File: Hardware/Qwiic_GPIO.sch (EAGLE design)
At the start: 31 parts, among them J2 SMD, J3 PTH, J4 SMD, U3 TCA9534U

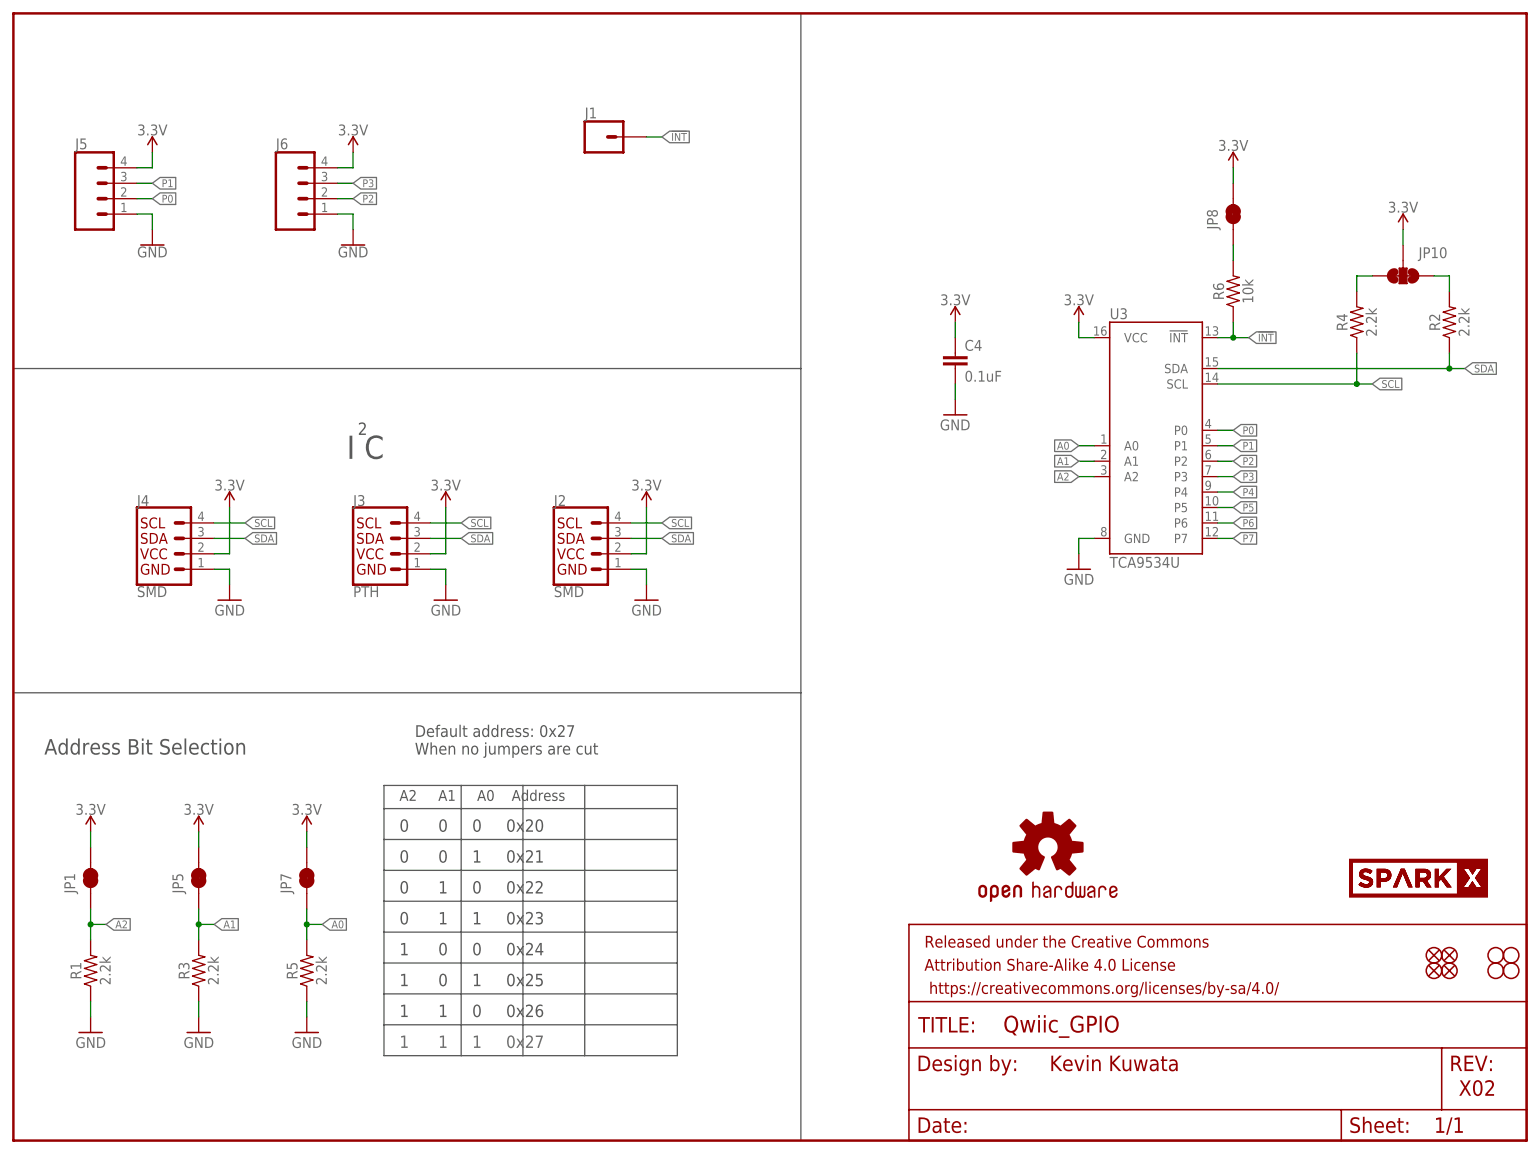
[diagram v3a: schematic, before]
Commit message: Change silk to table
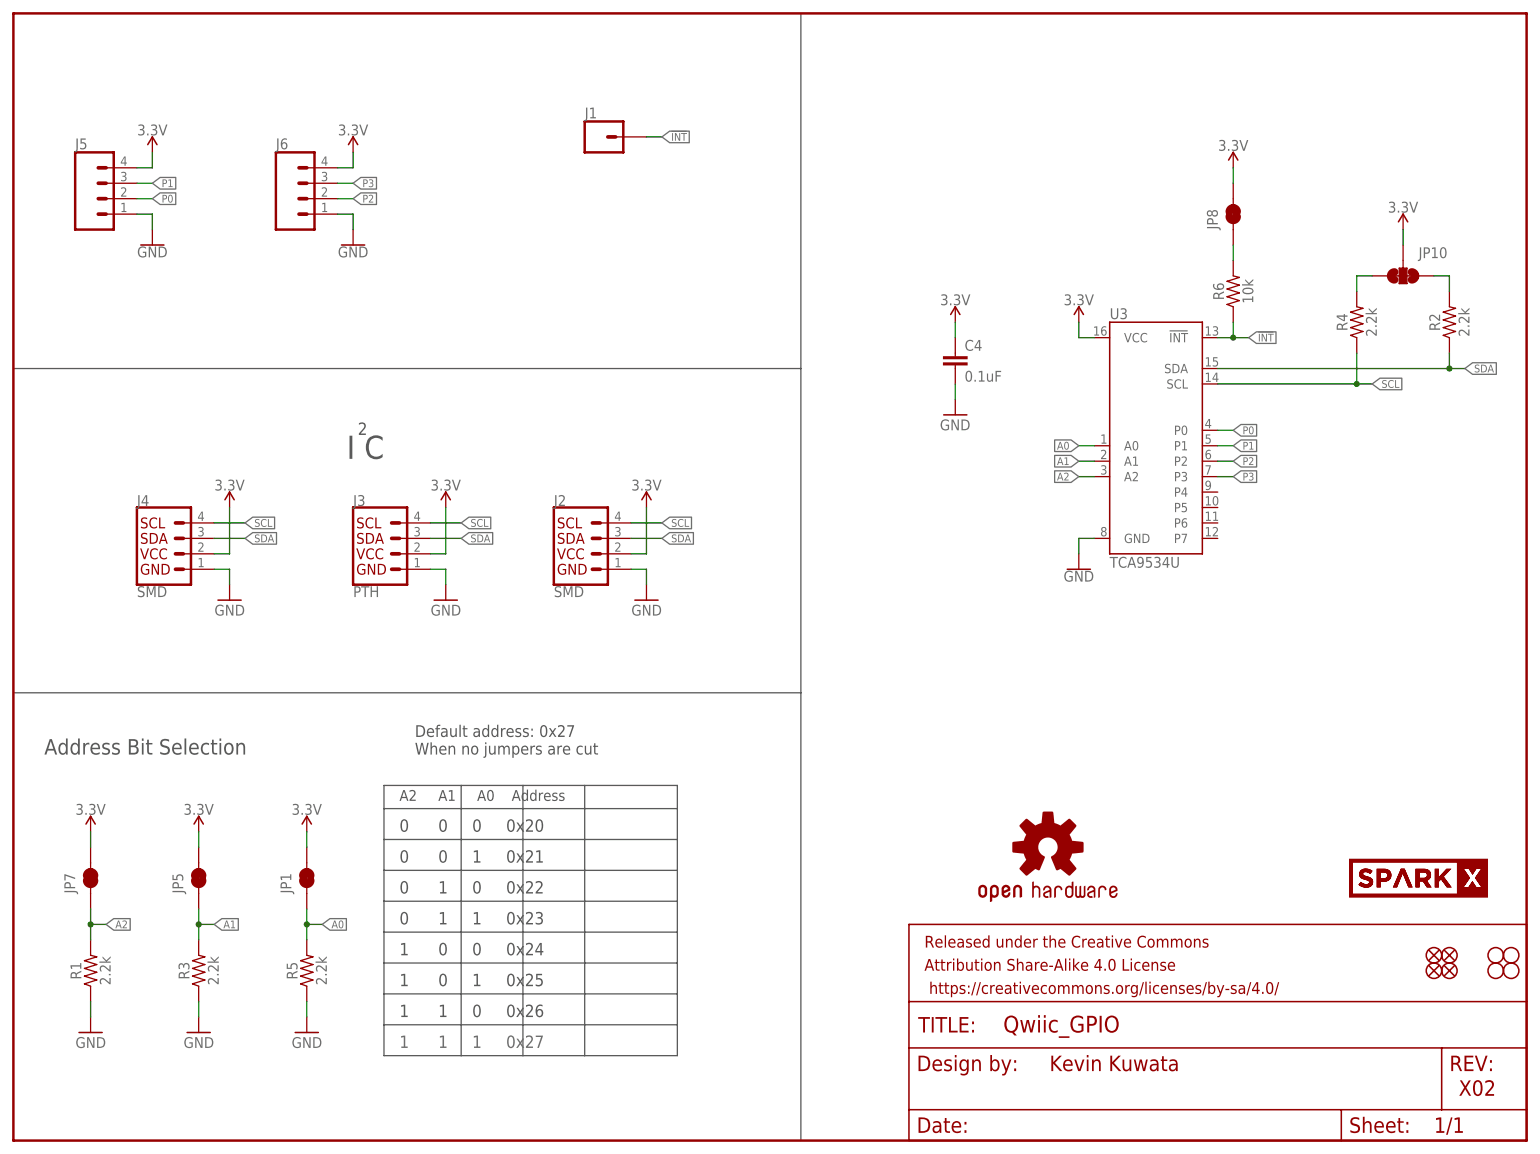
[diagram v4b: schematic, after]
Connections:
- removed net P4: U3.P4
- removed net P5: U3.P5
- removed net P6: U3.P6
- removed net P7: U3.P7
- net A0: now also JP1.1; no longer JP7.1
- net A2: now also JP7.1; no longer JP1.1
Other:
- moved on the sheet: JP1, JP7
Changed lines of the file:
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@@
 <?xml version="1.0" encoding="utf-8"?>
 <!DOCTYPE eagle SYSTEM "eagle.dtd">
-<eagle version="9.4.2">
+<eagle version="9.5.2">
 <drawing>
 <settings>
@@
 <part name="U3" library="KevinKuwata_eagle" deviceset="TCA9534" device="U"/>
 <part name="J1" library="SparkFun-Connectors" deviceset="CONN_01" device="PTH_NO_SILK_YES_STOP"/>
-<part name="JP1" library="SparkFun-Jumpers" deviceset="JUMPER-SMT_2_NC_TRACE" device="_SILK" package3d_urn="urn:adsk.eagle:package:39281/1" value="JUMPER-SMT_2_NC_TRACE_SILK"/>
 <part name="R1" library="SparkFun-Resistors" deviceset="2.2KOHM" device="-0603-1/10W-1%" value="2.2k"/>
 <part name="R3" library="SparkFun-Resistors" deviceset="2.2KOHM" device="-0603-1/10W-1%" value="2.2k"/>
@@
 <part name="GND2" library="SparkFun" deviceset="GND" device=""/>
 <part name="GND3" library="SparkFun" deviceset="GND" device=""/>
-<part name="JP5" library="SparkFun-Jumpers" deviceset="JUMPER-SMT_2_NC_TRACE" device="_SILK" package3d_urn="urn:adsk.eagle:package:39281/1" value="JUMPER-SMT_2_NC_TRACE_SILK"/>
-<part name="JP7" library="SparkFun-Jumpers" deviceset="JUMPER-SMT_2_NC_TRACE" device="_SILK" package3d_urn="urn:adsk.eagle:package:39281/1" value="JUMPER-SMT_2_NC_TRACE_SILK"/>
 <part name="SUPPLY2" library="SparkFun-PowerSymbols" deviceset="3.3V" device=""/>
 <part name="SUPPLY3" library="SparkFun-PowerSymbols" deviceset="3.3V" device=""/>
 <part name="SUPPLY6" library="SparkFun-PowerSymbols" deviceset="3.3V" device=""/>
-<part name="GND5" library="SparkFun" deviceset="GND" device=""/>
 <part name="SUPPLY9" library="SparkFun-PowerSymbols" deviceset="3.3V" device=""/>
 <part name="GND9" library="SparkFun-PowerSymbols" deviceset="GND" device=""/>
@@
 <part name="J6" library="SparkFun-Connectors" deviceset="CONN_04" device="LATCH"/>
 <part name="JP8" library="SparkFun-Jumpers" deviceset="JUMPER-SMT_2_NC_TRACE" device="_SILK" package3d_urn="urn:adsk.eagle:package:39281/1"/>
+<part name="GND11" library="SparkFun-PowerSymbols" deviceset="GND" device=""/>
+<part name="JP1" library="SparkFun-Jumpers" deviceset="JUMPER-SMT_2_NC_TRACE" device="_SILK" package3d_urn="urn:adsk.eagle:package:39281/1" value=""/>
+<part name="JP5" library="SparkFun-Jumpers" deviceset="JUMPER-SMT_2_NC_TRACE" device="_SILK" package3d_urn="urn:adsk.eagle:package:39281/1" value=""/>
+<part name="JP7" library="SparkFun-Jumpers" deviceset="JUMPER-SMT_2_NC_TRACE" device="_SILK" package3d_urn="urn:adsk.eagle:package:39281/1" value=""/>
 </parts>
 <sheets>
@@
 <attribute name="NAME" x="93.98" y="168.148" size="1.778" layer="95" font="vector"/>
 </instance>
-<instance part="JP1" gate="G$1" x="12.7" y="43.18" smashed="yes" rot="R90">
-<attribute name="NAME" x="10.16" y="40.64" size="1.778" layer="95" font="vector" rot="R90"/>
-</instance>
 <instance part="R1" gate="G$1" x="12.7" y="27.94" smashed="yes" rot="R90">
 <attribute name="NAME" x="11.176" y="27.94" size="1.778" layer="95" font="vector" rot="R90" align="bottom-center"/>
@@
 <attribute name="VALUE" x="50.8" y="15.24" size="1.778" layer="96" rot="MR0"/>
 </instance>
-<instance part="JP5" gate="G$1" x="30.48" y="43.18" smashed="yes" rot="R90">
-<attribute name="NAME" x="27.94" y="40.64" size="1.778" layer="95" font="vector" rot="R90"/>
-</instance>
-<instance part="JP7" gate="G$1" x="48.26" y="43.18" smashed="yes" rot="R90">
-<attribute name="NAME" x="45.72" y="40.64" size="1.778" layer="95" font="vector" rot="R90"/>
-</instance>
 <instance part="SUPPLY2" gate="G$1" x="12.7" y="50.8" smashed="yes" rot="MR0">
 <attribute name="VALUE" x="12.7" y="53.594" size="1.778" layer="96" rot="MR0" align="bottom-center"/>
@@
 <instance part="SUPPLY6" gate="G$1" x="48.26" y="50.8" smashed="yes" rot="MR0">
 <attribute name="VALUE" x="48.26" y="53.594" size="1.778" layer="96" rot="MR0" align="bottom-center"/>
-</instance>
-<instance part="GND5" gate="1" x="175.26" y="93.98" smashed="yes" rot="MR0">
-<attribute name="VALUE" x="177.8" y="91.44" size="1.778" layer="96" rot="MR0"/>
 </instance>
 <instance part="SUPPLY9" gate="G$1" x="175.26" y="134.62" smashed="yes">
@@
 <attribute name="NAME" x="198.12" y="149.86" size="1.778" layer="95" font="vector" rot="R90"/>
 </instance>
+<instance part="GND11" gate="1" x="175.26" y="93.98" smashed="yes">
+<attribute name="VALUE" x="175.26" y="93.726" size="1.778" layer="96" align="top-center"/>
+</instance>
+<instance part="JP1" gate="G$1" x="48.26" y="43.18" smashed="yes" rot="R90">
+<attribute name="NAME" x="45.72" y="40.64" size="1.778" layer="95" font="vector" rot="R90"/>
+<attribute name="VALUE" x="50.8" y="40.64" size="1.778" layer="96" font="vector" rot="R90" align="top-left"/>
+</instance>
+<instance part="JP5" gate="G$1" x="30.48" y="43.18" smashed="yes" rot="R90">
+<attribute name="NAME" x="27.94" y="40.64" size="1.778" layer="95" font="vector" rot="R90"/>
+<attribute name="VALUE" x="33.02" y="40.64" size="1.778" layer="96" font="vector" rot="R90" align="top-left"/>
+</instance>
+<instance part="JP7" gate="G$1" x="12.7" y="43.18" smashed="yes" rot="R90">
+<attribute name="NAME" x="10.16" y="40.64" size="1.778" layer="95" font="vector" rot="R90"/>
+<attribute name="VALUE" x="15.24" y="40.64" size="1.778" layer="96" font="vector" rot="R90" align="top-left"/>
+</instance>
 </instances>
 <busses>
@@
 </segment>
 <segment>
-<pinref part="JP1" gate="G$1" pin="2"/>
 <pinref part="SUPPLY2" gate="G$1" pin="3.3V"/>
 <wire x1="12.7" y1="48.26" x2="12.7" y2="50.8" width="0.1524" layer="91"/>
+<pinref part="JP7" gate="G$1" pin="2"/>
 </segment>
 <segment>
@@
 <wire x1="48.26" y1="48.26" x2="48.26" y2="50.8" width="0.1524" layer="91"/>
 <pinref part="SUPPLY6" gate="G$1" pin="3.3V"/>
-<pinref part="JP7" gate="G$1" pin="2"/>
+<pinref part="JP1" gate="G$1" pin="2"/>
 </segment>
 <segment>
@@
 </segment>
 <segment>
-<pinref part="U3" gate="U1" pin="GND"/>
-<wire x1="177.8" y1="99.06" x2="175.26" y2="99.06" width="0.1524" layer="91"/>
-<wire x1="175.26" y1="99.06" x2="175.26" y2="96.52" width="0.1524" layer="91"/>
-<pinref part="GND5" gate="1" pin="GND"/>
-</segment>
-<segment>
 <wire x1="20.32" y1="152.4" x2="22.86" y2="152.4" width="0.1524" layer="91"/>
 <wire x1="22.86" y1="152.4" x2="22.86" y2="149.86" width="0.1524" layer="91"/>
@@
 <pinref part="GND10" gate="1" pin="GND"/>
 <pinref part="J6" gate="J1" pin="1"/>
+</segment>
+<segment>
+<pinref part="U3" gate="U1" pin="GND"/>
+<wire x1="177.8" y1="99.06" x2="175.26" y2="99.06" width="0.1524" layer="91"/>
+<wire x1="175.26" y1="99.06" x2="175.26" y2="96.52" width="0.1524" layer="91"/>
+<pinref part="GND11" gate="1" pin="GND"/>
 </segment>
 </net>
@@
 <wire x1="48.26" y1="35.56" x2="48.26" y2="33.02" width="0.1524" layer="91"/>
 <junction x="48.26" y="35.56"/>
-<pinref part="JP7" gate="G$1" pin="1"/>
 <wire x1="48.26" y1="38.1" x2="48.26" y2="35.56" width="0.1524" layer="91"/>
+<pinref part="JP1" gate="G$1" pin="1"/>
 </segment>
 </net>
@@
 <wire x1="30.48" y1="33.02" x2="30.48" y2="35.56" width="0.1524" layer="91"/>
 <junction x="30.48" y="35.56"/>
+<wire x1="30.48" y1="38.1" x2="30.48" y2="35.56" width="0.1524" layer="91"/>
 <pinref part="JP5" gate="G$1" pin="1"/>
-<wire x1="30.48" y1="38.1" x2="30.48" y2="35.56" width="0.1524" layer="91"/>
 </segment>
 </net>
@@
 <wire x1="12.7" y1="35.56" x2="12.7" y2="33.02" width="0.1524" layer="91"/>
 <junction x="12.7" y="35.56"/>
-<pinref part="JP1" gate="G$1" pin="1"/>
 <wire x1="12.7" y1="35.56" x2="12.7" y2="38.1" width="0.1524" layer="91"/>
+<pinref part="JP7" gate="G$1" pin="1"/>
 </segment>
 </net>
@@
 </segment>
 </net>
-<net name="P4" class="0">
-<segment>
-<pinref part="U3" gate="U1" pin="P4"/>
-<wire x1="198.12" y1="106.68" x2="200.66" y2="106.68" width="0.1524" layer="91"/>
-<label x="200.66" y="106.68" size="1.27" layer="95" xref="yes"/>
-</segment>
-</net>
-<net name="P5" class="0">
-<segment>
-<pinref part="U3" gate="U1" pin="P5"/>
-<wire x1="198.12" y1="104.14" x2="200.66" y2="104.14" width="0.1524" layer="91"/>
-<label x="200.66" y="104.14" size="1.27" layer="95" xref="yes"/>
-</segment>
-</net>
-<net name="P6" class="0">
-<segment>
-<pinref part="U3" gate="U1" pin="P6"/>
-<wire x1="198.12" y1="101.6" x2="200.66" y2="101.6" width="0.1524" layer="91"/>
-<label x="200.66" y="101.6" size="1.27" layer="95" xref="yes"/>
-</segment>
-</net>
-<net name="P7" class="0">
-<segment>
-<pinref part="U3" gate="U1" pin="P7"/>
-<wire x1="198.12" y1="99.06" x2="200.66" y2="99.06" width="0.1524" layer="91"/>
-<label x="200.66" y="99.06" size="1.27" layer="95" xref="yes"/>
-</segment>
-</net>

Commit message: Added missing product ID's
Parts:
- J2, J4: PROD_ID (none) -> CONN-13694
- J5, J6: PROD_ID (none) -> CON-14722
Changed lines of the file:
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@@
 <part name="SUPPLY4" library="SparkFun-PowerSymbols" deviceset="3.3V" device=""/>
 <part name="SUPPLY5" library="SparkFun-PowerSymbols" deviceset="3.3V" device=""/>
-<part name="J2" library="SparkX" deviceset="I2C_STANDARD" device="JS-1MM" value="SMD"/>
+<part name="J2" library="SparkX" deviceset="I2C_STANDARD" device="JS-1MM" value="SMD">
+<attribute name="PROD_ID" value="CONN-13694"/>
+</part>
 <part name="SUPPLY7" library="SparkFun-PowerSymbols" deviceset="3.3V" device=""/>
 <part name="J3" library="SparkX" deviceset="I2C_STANDARD" device="_NO_SILK" value="PTH"/>
@@
 <part name="C4" library="SparkFun-Capacitors" deviceset="0.1UF" device="-0603-25V-(+80/-20%)" value="0.1uF"/>
 <part name="SUPPLY8" library="SparkFun-PowerSymbols" deviceset="3.3V" device=""/>
-<part name="J4" library="SparkX" deviceset="I2C_STANDARD" device="JS-1MM" value="SMD"/>
+<part name="J4" library="SparkX" deviceset="I2C_STANDARD" device="JS-1MM" value="SMD">
+<attribute name="PROD_ID" value="CONN-13694"/>
+</part>
 <part name="LOGO1" library="SparkFun-Aesthetics" deviceset="OSHW-LOGO" device="MINI"/>
 <part name="U$1" library="SparkX" deviceset="SPARKX-LOGO" device="3" value="SPARKX-LOGO3"/>
@@
 <part name="R6" library="SparkFun-Resistors" deviceset="10KOHM" device="-0603-1/10W-1%" value="10k"/>
 <part name="SUPPLY12" library="SparkFun-PowerSymbols" deviceset="3.3V" device=""/>
-<part name="J5" library="SparkFun-Connectors" deviceset="CONN_04" device="LATCH"/>
-<part name="J6" library="SparkFun-Connectors" deviceset="CONN_04" device="LATCH"/>
+<part name="J5" library="SparkFun-Connectors" deviceset="CONN_04" device="LATCH">
+<attribute name="PROD_ID" value="CON-14722"/>
+</part>
+<part name="J6" library="SparkFun-Connectors" deviceset="CONN_04" device="LATCH">
+<attribute name="PROD_ID" value="CON-14722"/>
+</part>
 <part name="JP8" library="SparkFun-Jumpers" deviceset="JUMPER-SMT_2_NC_TRACE" device="_SILK" package3d_urn="urn:adsk.eagle:package:39281/1"/>
 <part name="GND11" library="SparkFun-PowerSymbols" deviceset="GND" device=""/>
@@
 <attribute name="VALUE" x="88.9" y="91.186" size="1.778" layer="96" font="vector" align="top-left"/>
 <attribute name="NAME" x="88.9" y="104.394" size="1.778" layer="95" font="vector"/>
+<attribute name="PROD_ID" x="93.98" y="96.52" size="1.27" layer="96" display="off"/>
 </instance>
 <instance part="SUPPLY7" gate="G$1" x="71.12" y="104.14" smashed="yes" rot="MR0">
@@
 <attribute name="VALUE" x="20.32" y="91.186" size="1.778" layer="96" font="vector" align="top-left"/>
 <attribute name="NAME" x="20.32" y="104.394" size="1.778" layer="95" font="vector"/>
+<attribute name="PROD_ID" x="25.4" y="96.52" size="1.27" layer="96" display="off"/>
 </instance>
 <instance part="LOGO1" gate="G$1" x="170.18" y="48.26" smashed="yes"/>

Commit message: Added PWR LED, made labels larger
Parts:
- added 3V3: JUMPER-SMT_2_NC_TRACE_SILK, SparkFun-Jumpers:JUMPER-SMT_2_NC_TRACE_SILK
- added D1: RED, SparkFun-LED:LED-RED0603
- added R7: 1k, SparkFun-Resistors:1KOHM-0603-1/10W-1%
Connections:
- new net N$2: D1.A, R7.1
- new net N$3: 3V3.1, R7.2
- net 3.3V: now also 3V3.2
- net GND: now also D1.C
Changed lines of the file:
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@@
 <part name="GND6" library="SparkFun-PowerSymbols" deviceset="GND" device=""/>
 <part name="GND7" library="SparkFun-PowerSymbols" deviceset="GND" device=""/>
+<part name="SUPPLY13" library="SparkFun-PowerSymbols" deviceset="3.3V" device=""/>
+<part name="3V3" library="SparkFun-Jumpers" deviceset="JUMPER-SMT_2_NC_TRACE" device="_SILK" package3d_urn="urn:adsk.eagle:package:39281/1"/>
+<part name="R7" library="SparkFun-Resistors" deviceset="1KOHM" device="-0603-1/10W-1%" value="1k"/>
+<part name="D1" library="SparkFun-LED" deviceset="LED-RED" device="0603" value="RED"/>
+<part name="GND8" library="SparkFun-PowerSymbols" deviceset="GND" device=""/>
 </parts>
 <sheets>
@@
 <attribute name="VALUE" x="154.94" y="119.126" size="1.778" layer="96" align="top-center"/>
 </instance>
+<instance part="SUPPLY13" gate="G$1" x="142.24" y="86.36" smashed="yes">
+<attribute name="VALUE" x="142.24" y="89.154" size="1.778" layer="96" align="bottom-center"/>
+</instance>
+<instance part="3V3" gate="G$1" x="142.24" y="78.74" smashed="yes" rot="R90">
+<attribute name="NAME" x="139.7" y="76.2" size="1.778" layer="95" font="vector" rot="R90"/>
+</instance>
+<instance part="R7" gate="G$1" x="142.24" y="66.04" smashed="yes" rot="R90">
+<attribute name="NAME" x="140.716" y="66.04" size="1.778" layer="95" font="vector" rot="R90" align="bottom-center"/>
+<attribute name="VALUE" x="143.764" y="66.04" size="1.778" layer="96" font="vector" rot="R90" align="top-center"/>
+</instance>
+<instance part="D1" gate="G$1" x="142.24" y="55.88" smashed="yes">
+<attribute name="NAME" x="138.811" y="51.308" size="1.778" layer="95" font="vector" rot="R90"/>
+<attribute name="VALUE" x="144.145" y="51.308" size="1.778" layer="96" font="vector" rot="R90" align="top-left"/>
+</instance>
+<instance part="GND8" gate="1" x="142.24" y="45.72" smashed="yes">
+<attribute name="VALUE" x="142.24" y="45.466" size="1.778" layer="96" align="top-center"/>
+</instance>
 </instances>
 <busses>
@@
 <wire x1="200.66" y1="160.02" x2="200.66" y2="157.48" width="0.1524" layer="91"/>
 </segment>
+<segment>
+<pinref part="3V3" gate="G$1" pin="2"/>
+<pinref part="SUPPLY13" gate="G$1" pin="3.3V"/>
+<wire x1="142.24" y1="83.82" x2="142.24" y2="86.36" width="0.1524" layer="91"/>
+</segment>
 </net>
 <net name="GND" class="0">
@@
 <pinref part="C4" gate="G$1" pin="2"/>
 <pinref part="GND7" gate="1" pin="GND"/>
+</segment>
+<segment>
+<pinref part="GND8" gate="1" pin="GND"/>
+<pinref part="D1" gate="G$1" pin="C"/>
+<wire x1="142.24" y1="48.26" x2="142.24" y2="50.8" width="0.1524" layer="91"/>
 </segment>
 </net>
@@
 </segment>
 </net>
+<net name="N$2" class="0">
+<segment>
+<pinref part="D1" gate="G$1" pin="A"/>
+<pinref part="R7" gate="G$1" pin="1"/>
+<wire x1="142.24" y1="58.42" x2="142.24" y2="60.96" width="0.1524" layer="91"/>
+</segment>
+</net>
+<net name="N$3" class="0">
+<segment>
+<pinref part="R7" gate="G$1" pin="2"/>
+<pinref part="3V3" gate="G$1" pin="1"/>
+<wire x1="142.24" y1="71.12" x2="142.24" y2="73.66" width="0.1524" layer="91"/>
+</segment>
+</net>

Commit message: Generated new panel file
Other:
- note added: "X03"
- note removed: "X02"
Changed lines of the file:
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@@
 <plain>
 <text x="170.434" y="11.43" size="2.54" layer="94">Kevin Kuwata</text>
-<text x="237.744" y="7.366" size="2.54" layer="94">X02</text>
+<text x="237.744" y="7.366" size="2.54" layer="94">X03</text>
 <text x="57.912" y="114.046" size="3.81" layer="97" align="center">I C</text>
 <text x="5.08" y="63.5" size="2.54" layer="97">Address Bit Selection
